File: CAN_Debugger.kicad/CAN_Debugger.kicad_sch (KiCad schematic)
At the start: 174 parts, among them J1 Conn_01x02, J15 RS-485, J16 RS-485, J2 Conn_01x04_MountingPin, J3 Conn_01x02, J4 Conn_01x16_Socket, J4 USB_C_Receptacle_USB2.0, J6 RS-485, J7 CAN, J8 CAN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

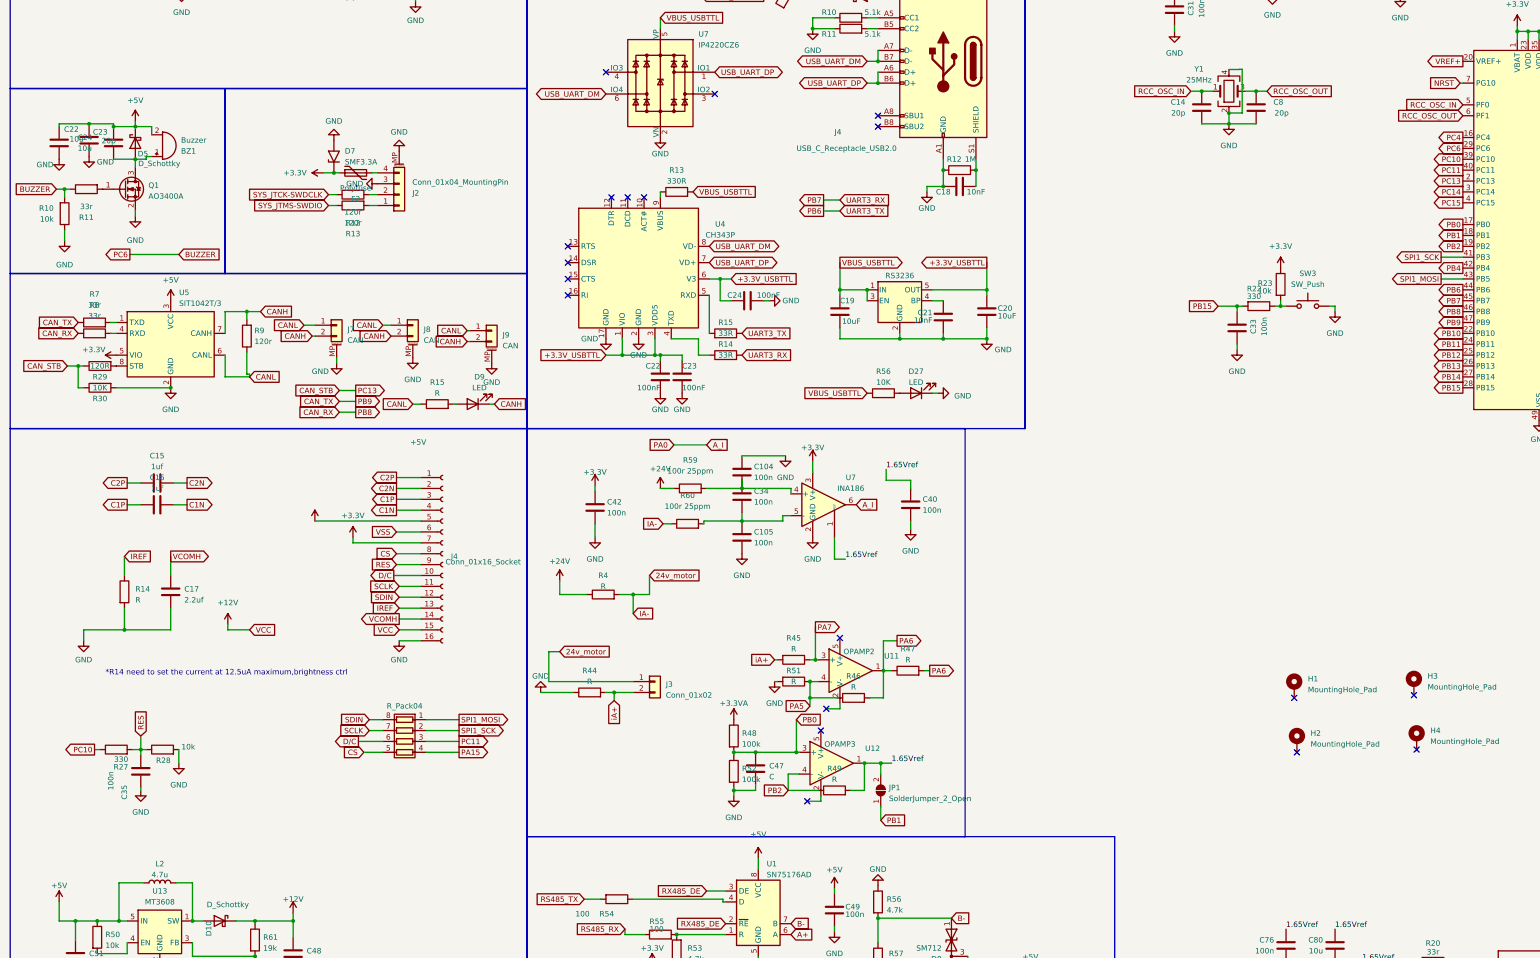
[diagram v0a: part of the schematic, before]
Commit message: Generated Code from CubeMX and CLion
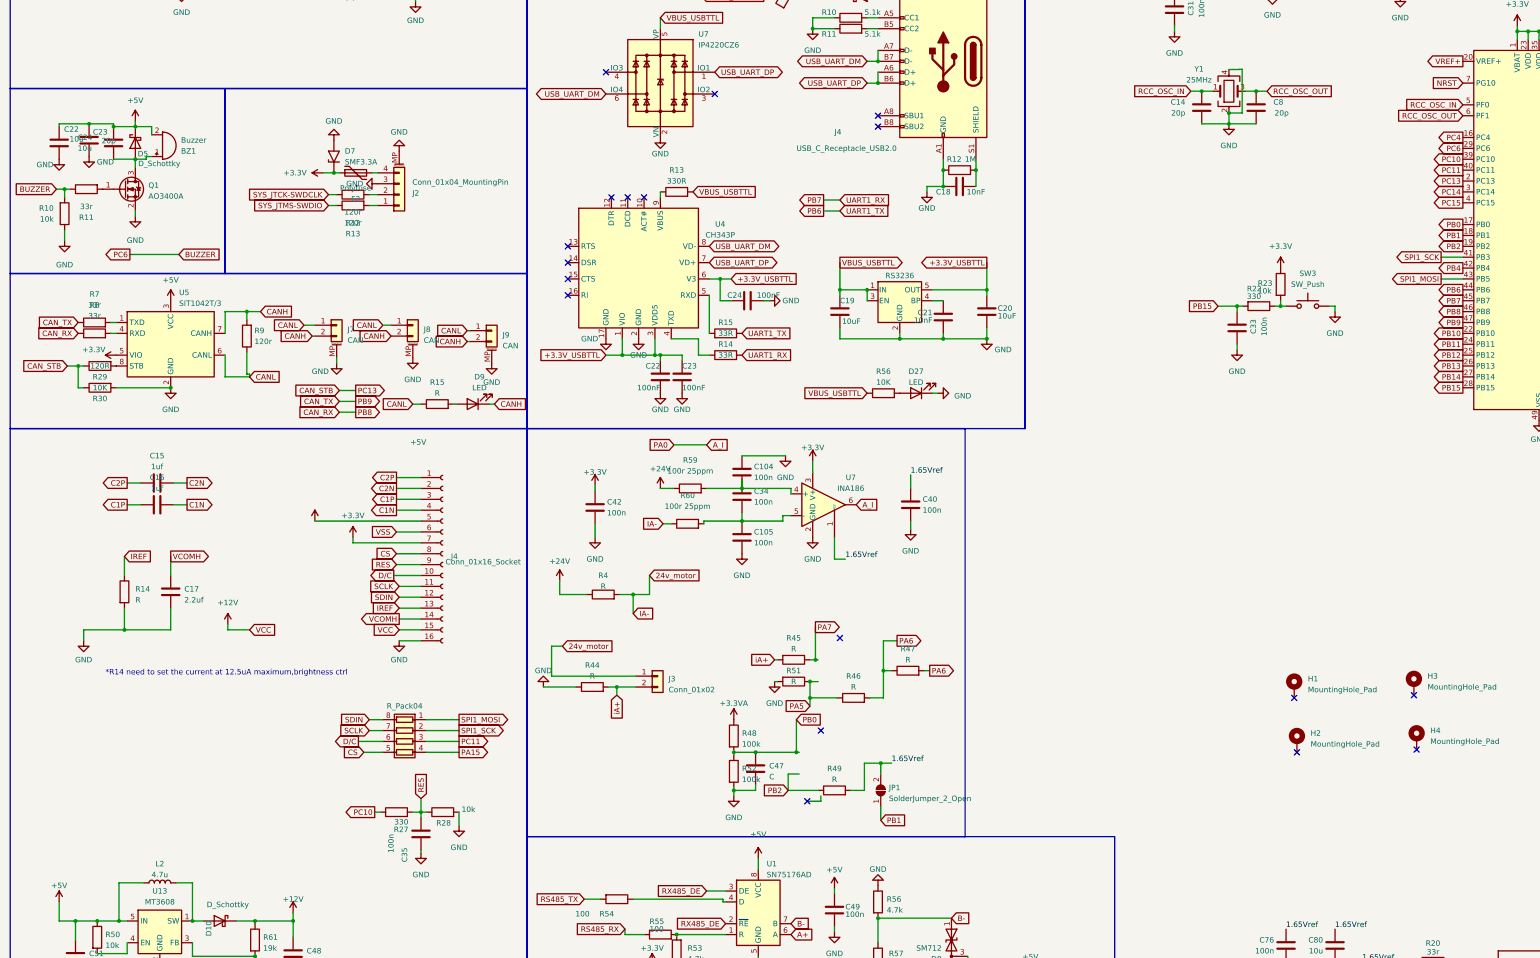
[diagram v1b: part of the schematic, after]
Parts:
- removed U11: OPAMP2, Package_TO_SOT_SMD:TSOT-23-5, symbol Amplifier_Operational:AD8603
- removed U12: OPAMP3, Package_TO_SOT_SMD:TSOT-23-5, symbol Amplifier_Operational:AD8603
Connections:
- no-connect marks 19 -> 18
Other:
- moved on the sheet: C35, J3, R27, R28, R44
